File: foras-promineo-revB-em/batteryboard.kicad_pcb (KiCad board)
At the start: 2 copper layers, 90.2 x 101.1 mm, 48 parts, among them J101 KEYSTONE-1042, J102 KEYSTONE-1042, J103 KEYSTONE-1042, J104 KEYSTONE-1042, J105 KEYSTONE-1042, J106 KEYSTONE-1042, J107 Conn_02x10_Top_Bottom, P201 Conn_02x60_Top_Bottom, Q101 IRF7458, Q102 IRF7458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

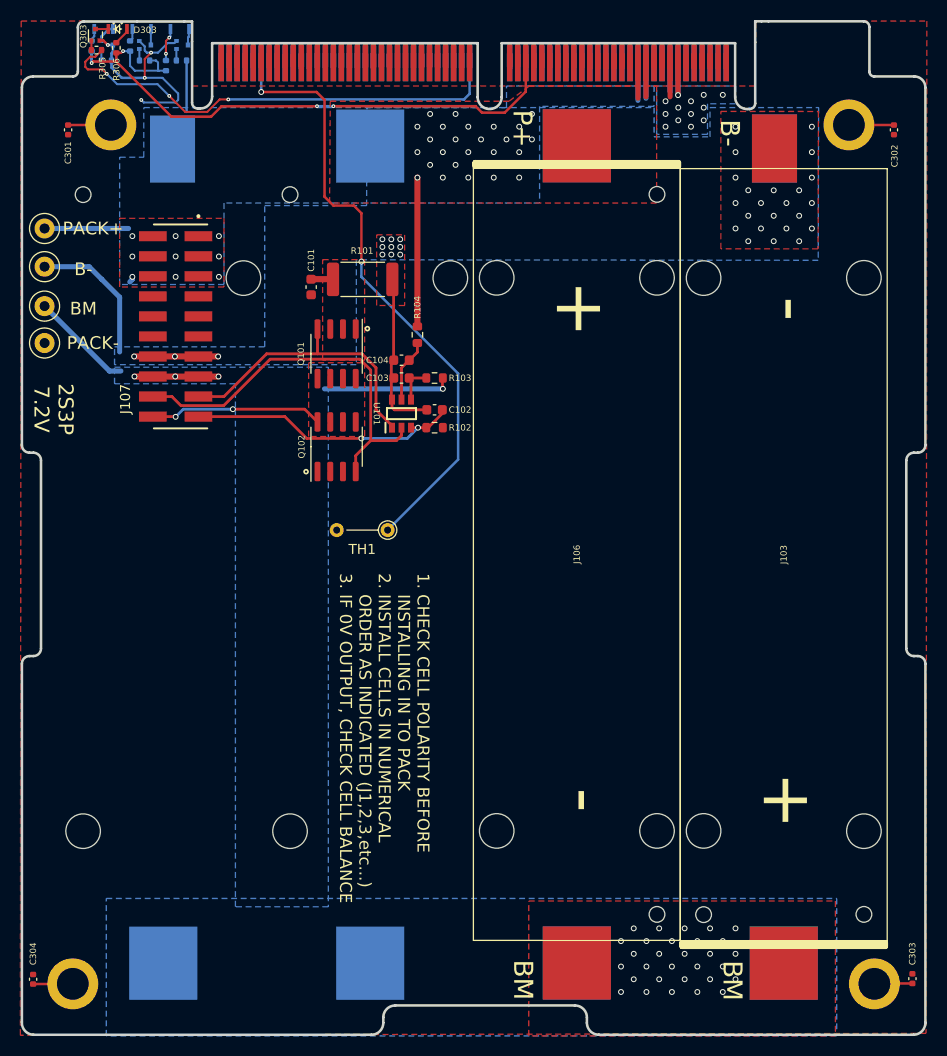
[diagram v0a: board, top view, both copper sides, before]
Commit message: Thermal relief and Pours
changed thermal reliefs to solid. Changed a few pour clearances.
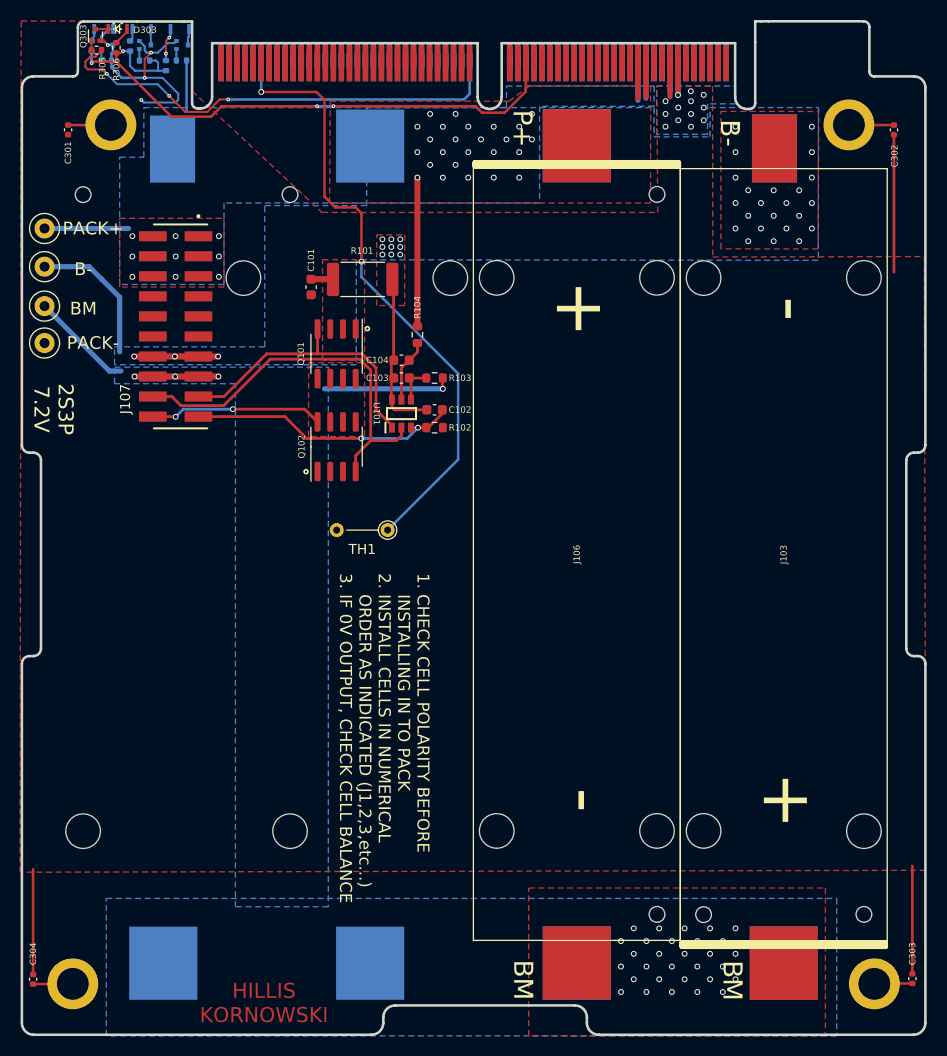
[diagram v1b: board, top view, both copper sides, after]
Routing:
- net PACK-: track 34.6 -> 69.7 mm
- net PACK+: track 41.5 -> 40.9 mm

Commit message: final changes before fab
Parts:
- added G***: LOGO, batteryboard:SLI_LOGO, F.Cu at (72.9, 134.1)
- added Ref**: Val**, custom-footprints:battery_version, F.Cu at (75.2, 140.7)
- J101: footprint batteryboard-v01b_SLI_card:KEYSTONE-1042_ALT_J1 -> batteryboard:KEYSTONE-1042_ALT_J1
- J102, J104, J106: footprint batteryboard-v01b_SLI_card:KEYSTONE-1042 -> batteryboard:KEYSTONE-1042
- J103: footprint batteryboard-v01b_SLI_card:KEYSTONE-1042_ALT_J5 -> batteryboard:KEYSTONE-1042_ALT_J5
- J105: footprint batteryboard-v01b_SLI_card:KEYSTONE-1042_alt_J4 -> batteryboard:KEYSTONE-1042_alt_J4
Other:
- board text added: "SIERRA LOBO INC."
- board text added: "revB-em"
